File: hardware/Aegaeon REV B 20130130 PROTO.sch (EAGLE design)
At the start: 39 parts, among them IC1 ATTINY84A-MMH, Q1 DMN65D8LDW, U1 V_REG_LDOSMD

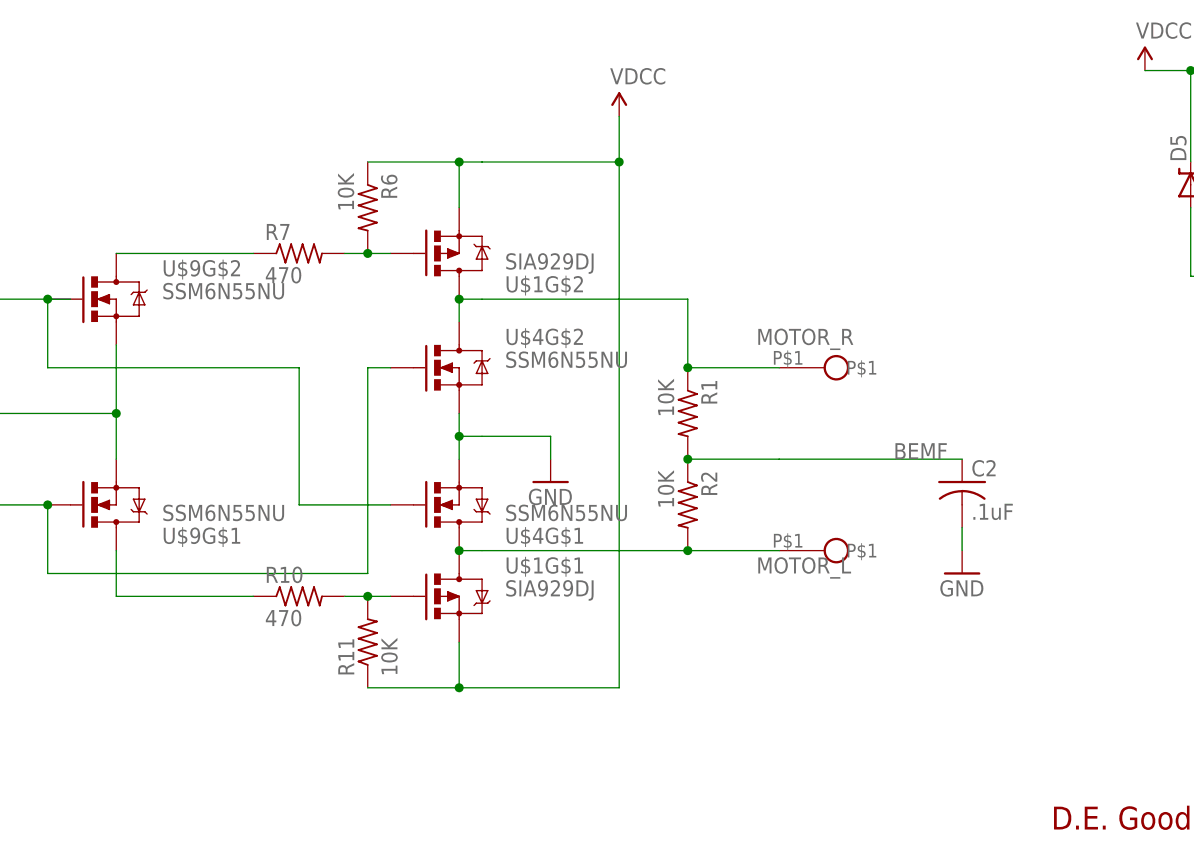
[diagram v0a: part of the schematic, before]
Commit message: Initial commit for H-Bridge designed with SI5504DC parts.
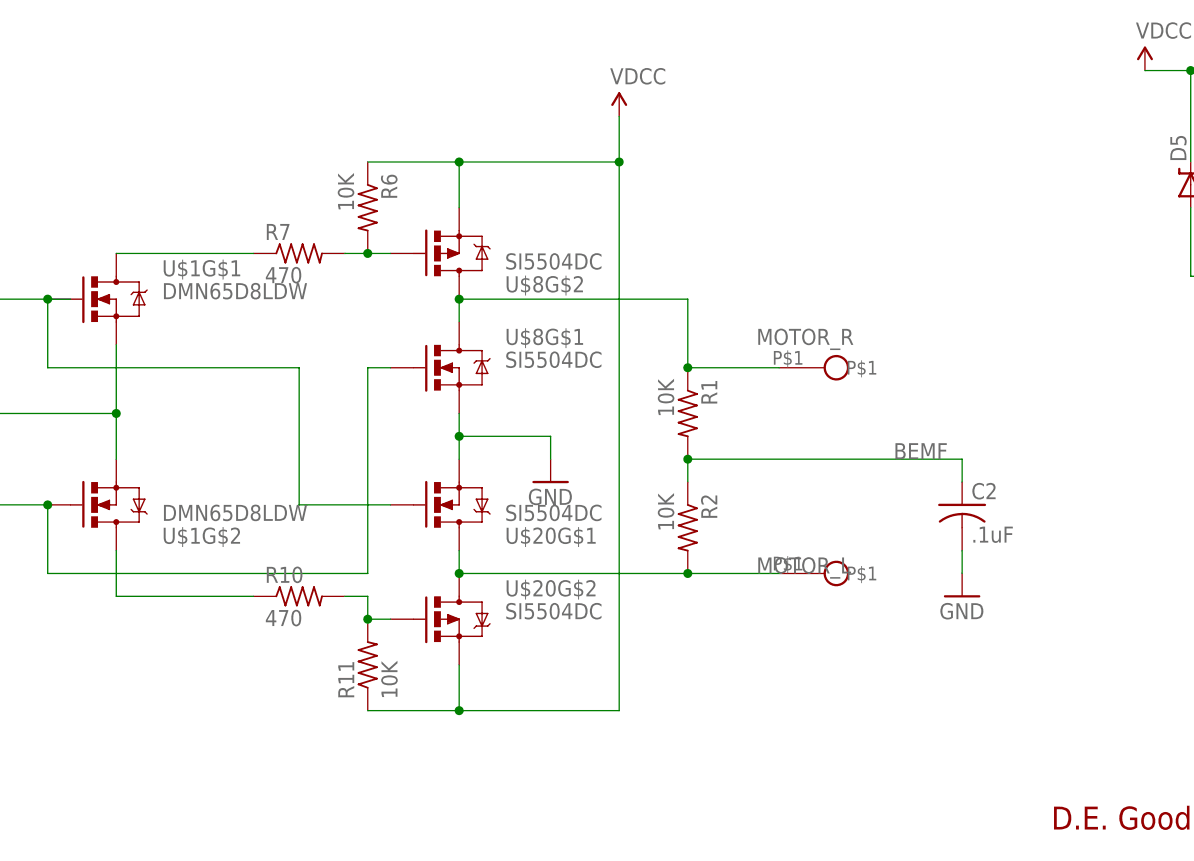
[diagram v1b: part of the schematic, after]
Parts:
- removed U$4, U$9: SSM6N55NU, Railstars:SSM6N55NU
- added U$20, U$8: SI5504DC, Railstars:SI5504DC
- U$1: value SIA929DJ -> DMN65D8LDW; device Railstars:SIA929DJ -> Railstars:DMN65D8LDW
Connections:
- net FORWARD: now also U$1G$1.G, U$20G$1.G; no longer U$4G$1.G, U$9G$2.G
- net GND: now also U$20G$1.S, U$8G$1.S; no longer U$4G$1.S, U$4G$2.S
- net MOTOR_L: now also U$20G$1.D, U$20G$2.D; no longer U$1G$1.D, U$4G$1.D
- net MOTOR_R: now also U$8G$1.D, U$8G$2.D; no longer U$1G$2.D, U$4G$2.D
- net N$1: now also U$8G$2.G; no longer U$1G$2.G
- net N$10: now also U$1G$2.D; no longer U$9G$1.D
- net N$11: now also U$1G$1.D; no longer U$9G$2.D
- net N$4: now also U$20G$2.G; no longer U$1G$1.G
- net PWM: now also U$1G$1.S, U$1G$2.S; no longer U$9G$1.S, U$9G$2.S
- net REVERSE: now also U$1G$2.G, U$8G$1.G; no longer U$4G$2.G, U$9G$1.G
- net VDCC: now also U$20G$2.S, U$8G$2.S; no longer U$1G$1.S, U$1G$2.S
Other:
- moved on the sheet: C2, R11, R2, U$1G$1, U$1G$2

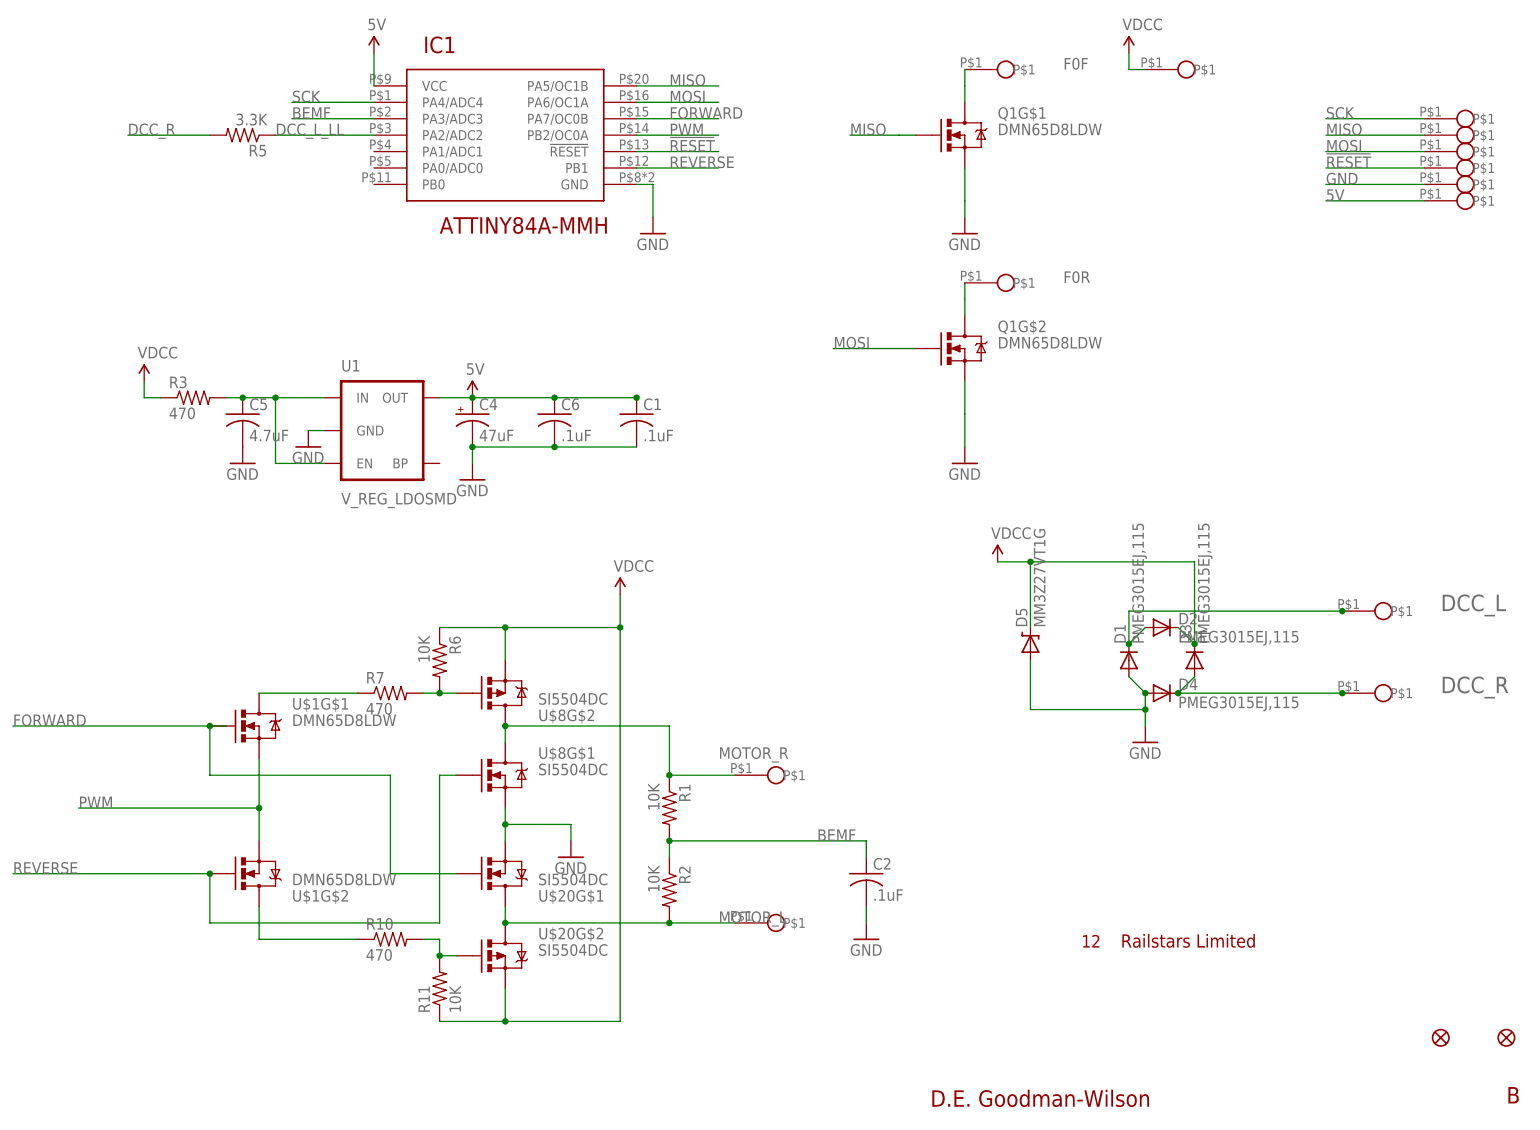
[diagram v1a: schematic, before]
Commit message: Redesigning the H-Bridge. This one seems to work under test.
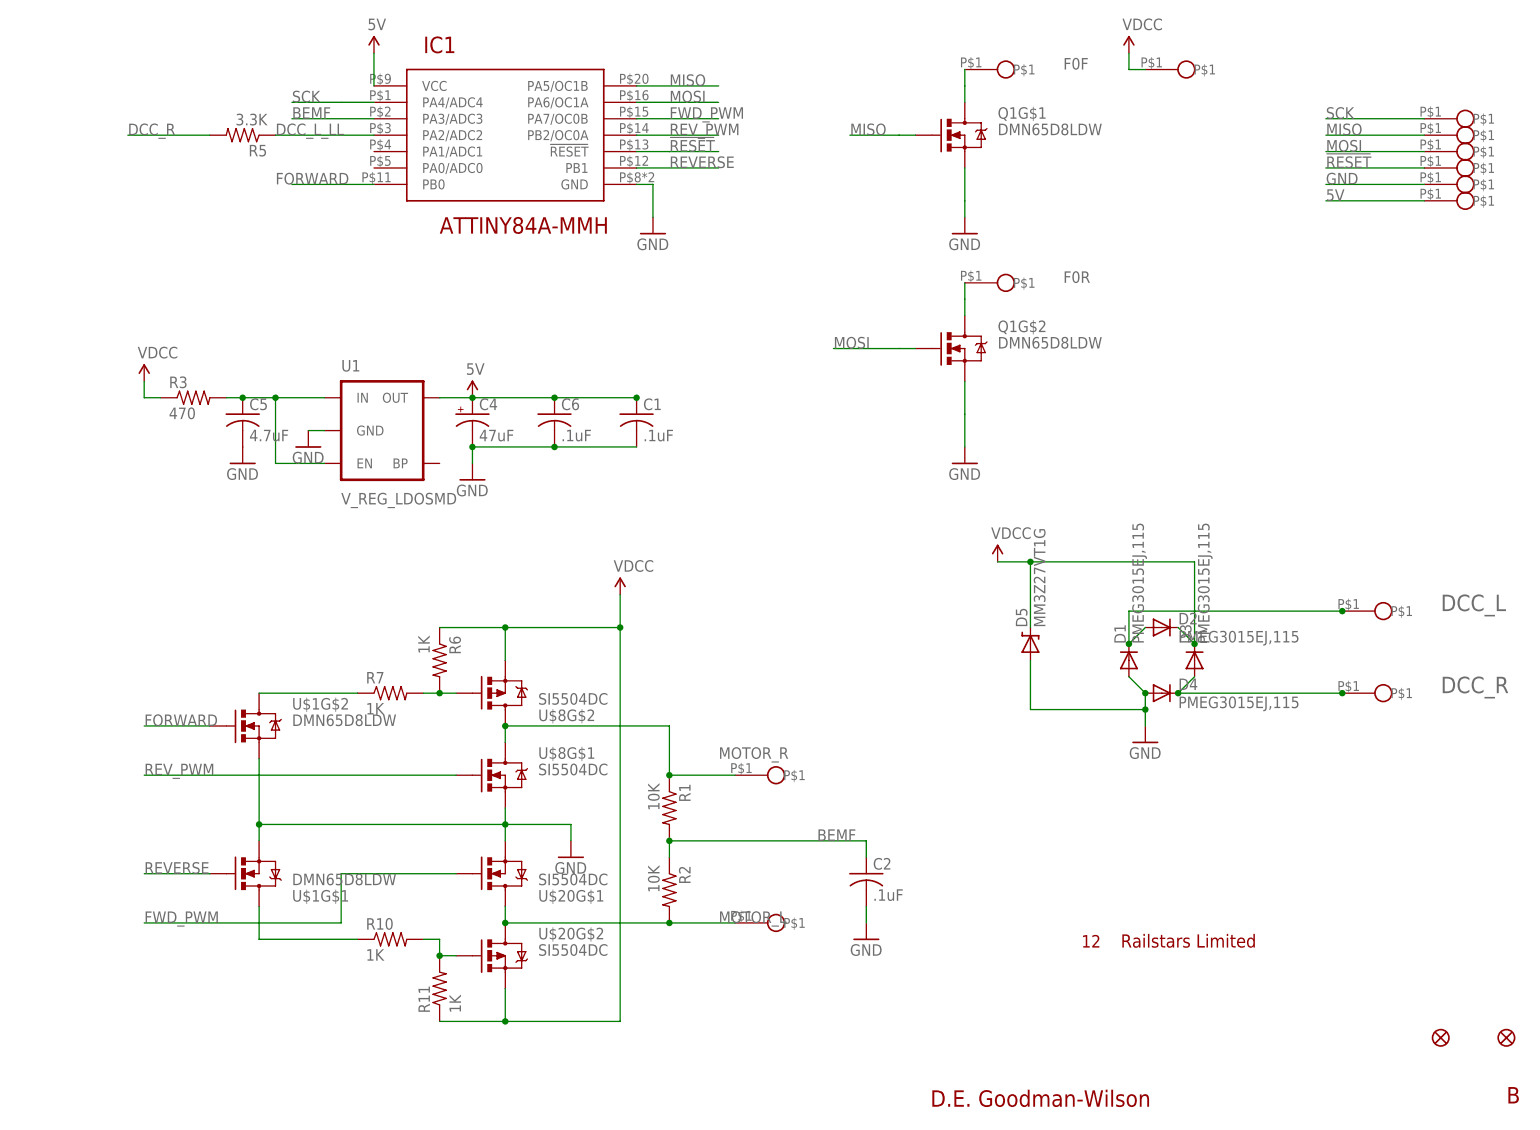
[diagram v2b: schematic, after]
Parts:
- R10, R7: value 470 -> 1K
- R11, R6: value 10K -> 1K
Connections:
- removed net PWM: IC1.PB2/OC0A, U$1G$1.S, U$1G$2.S
- new net FWD_PWM: IC1.PA7/OC0B, U$20G$1.G
- new net REV_PWM: IC1.PB2/OC0A, U$8G$1.G
- net FORWARD: now also IC1.PB0, U$1G$2.G; no longer IC1.PA7/OC0B, U$1G$1.G, U$20G$1.G
- net GND: now also U$1G$1.S, U$1G$2.S
- net N$10: now also U$1G$1.D; no longer U$1G$2.D
- net N$11: now also U$1G$2.D; no longer U$1G$1.D
- net REVERSE: now also U$1G$1.G; no longer U$1G$2.G, U$8G$1.G
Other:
- moved on the sheet: U$1G$1, U$1G$2
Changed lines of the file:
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@@
 <part name="U$7" library="Railstars" deviceset="VDCC" device=""/>
 <part name="GND8" library="SparkFun-Aesthetics" deviceset="GND" device=""/>
-<part name="R6" library="rcl" deviceset="R-US_" device="R0201" value="10K"/>
-<part name="R7" library="rcl" deviceset="R-US_" device="R0201" value="470"/>
-<part name="R10" library="rcl" deviceset="R-US_" device="R0201" value="470"/>
-<part name="R11" library="rcl" deviceset="R-US_" device="R0201" value="10K"/>
+<part name="R6" library="rcl" deviceset="R-US_" device="R0201" value="1K"/>
+<part name="R7" library="rcl" deviceset="R-US_" device="R0201" value="1K"/>
+<part name="R10" library="rcl" deviceset="R-US_" device="R0201" value="1K"/>
+<part name="R11" library="rcl" deviceset="R-US_" device="R0201" value="1K"/>
 <part name="U1" library="SparkFun-PowerIC" deviceset="V_REG_LDO" device="SMD"/>
 <part name="D5" library="SparkFun-DiscreteSemi" deviceset="DIODE-ZENER" device="-BZT52" value="MM3Z27VT1G"/>
@@
 <instance part="U$20" gate="G$1" x="83.82" y="43.18" rot="MR180"/>
 <instance part="U$20" gate="G$2" x="83.82" y="30.48"/>
-<instance part="U$1" gate="G$1" x="45.72" y="66.04"/>
-<instance part="U$1" gate="G$2" x="45.72" y="43.18" rot="MR180"/>
+<instance part="U$1" gate="G$1" x="45.72" y="43.18" rot="MR180"/>
+<instance part="U$1" gate="G$2" x="45.72" y="66.04"/>
 </instances>
 <busses>
@@
 <wire x1="83.82" y1="48.26" x2="83.82" y2="50.8" width="0.1524" layer="91"/>
 <junction x="83.82" y="50.8"/>
+<wire x1="83.82" y1="50.8" x2="45.72" y2="50.8" width="0.1524" layer="91"/>
+<pinref part="U$1" gate="G$1" pin="S"/>
+<wire x1="45.72" y1="48.26" x2="45.72" y2="50.8" width="0.1524" layer="91"/>
+<pinref part="U$1" gate="G$2" pin="S"/>
+<wire x1="45.72" y1="60.96" x2="45.72" y2="50.8" width="0.1524" layer="91"/>
+<junction x="45.72" y="50.8"/>
 </segment>
 <segment>
@@
 <net name="REVERSE" class="0">
 <segment>
-<wire x1="38.1" y1="43.18" x2="7.62" y2="43.18" width="0.1524" layer="91"/>
-<wire x1="73.66" y1="58.42" x2="73.66" y2="35.56" width="0.1524" layer="91"/>
-<wire x1="73.66" y1="35.56" x2="38.1" y2="35.56" width="0.1524" layer="91"/>
-<wire x1="38.1" y1="35.56" x2="38.1" y2="43.18" width="0.1524" layer="91"/>
-<label x="7.62" y="43.18" size="1.778" layer="95"/>
-<pinref part="U$1" gate="G$2" pin="G"/>
-<junction x="38.1" y="43.18"/>
-<pinref part="U$8" gate="G$1" pin="G"/>
-<wire x1="73.66" y1="58.42" x2="76.2" y2="58.42" width="0.1524" layer="91"/>
-</segment>
-<segment>
 <label x="109.22" y="152.4" size="1.778" layer="95"/>
 <wire x1="104.14" y1="152.4" x2="116.84" y2="152.4" width="0.1524" layer="91"/>
 <pinref part="IC1" gate="G$1" pin="PB1"/>
 </segment>
-</net>
-<net name="FORWARD" class="0">
-<segment>
-<wire x1="40.64" y1="66.04" x2="38.1" y2="66.04" width="0.1524" layer="91"/>
-<wire x1="38.1" y1="66.04" x2="7.62" y2="66.04" width="0.1524" layer="91"/>
-<wire x1="66.04" y1="43.18" x2="66.04" y2="58.42" width="0.1524" layer="91"/>
-<wire x1="66.04" y1="58.42" x2="38.1" y2="58.42" width="0.1524" layer="91"/>
-<wire x1="38.1" y1="58.42" x2="38.1" y2="66.04" width="0.1524" layer="91"/>
-<junction x="38.1" y="66.04"/>
-<label x="7.62" y="66.04" size="1.778" layer="95"/>
+<segment>
+<label x="27.94" y="43.18" size="1.778" layer="95"/>
+<wire x1="38.1" y1="43.18" x2="27.94" y2="43.18" width="0.1524" layer="91"/>
 <pinref part="U$1" gate="G$1" pin="G"/>
-<pinref part="U$20" gate="G$1" pin="G"/>
-<wire x1="76.2" y1="43.18" x2="66.04" y2="43.18" width="0.1524" layer="91"/>
-</segment>
+</segment>
+</net>
+<net name="FWD_PWM" class="0">
 <segment>
 <pinref part="IC1" gate="G$1" pin="PA7/OC0B"/>
 <wire x1="104.14" y1="160.02" x2="116.84" y2="160.02" width="0.1524" layer="91"/>
 <label x="109.22" y="160.02" size="1.778" layer="95"/>
+</segment>
+<segment>
+<pinref part="U$20" gate="G$1" pin="G"/>
+<wire x1="76.2" y1="43.18" x2="58.42" y2="43.18" width="0.1524" layer="91"/>
+<wire x1="58.42" y1="43.18" x2="58.42" y2="35.56" width="0.1524" layer="91"/>
+<wire x1="58.42" y1="35.56" x2="27.94" y2="35.56" width="0.1524" layer="91"/>
+<label x="27.94" y="35.56" size="1.778" layer="95"/>
 </segment>
 </net>
@@
 <pinref part="R10" gate="G$1" pin="1"/>
 <wire x1="45.72" y1="33.02" x2="60.96" y2="33.02" width="0.1524" layer="91"/>
-<wire x1="45.72" y1="38.1" x2="45.72" y2="33.02" width="0.1524" layer="91"/>
-<pinref part="U$1" gate="G$2" pin="D"/>
+<pinref part="U$1" gate="G$1" pin="D"/>
+<wire x1="45.72" y1="33.02" x2="45.72" y2="38.1" width="0.1524" layer="91"/>
 </segment>
 </net>
@@
 <pinref part="R7" gate="G$1" pin="1"/>
 <wire x1="45.72" y1="71.12" x2="60.96" y2="71.12" width="0.1524" layer="91"/>
-<pinref part="U$1" gate="G$1" pin="D"/>
+<pinref part="U$1" gate="G$2" pin="D"/>
 </segment>
 </net>
@@
 </segment>
 </net>
-<net name="PWM" class="0">
-<segment>
-<wire x1="45.72" y1="60.96" x2="45.72" y2="53.34" width="0.1524" layer="91"/>
-<wire x1="45.72" y1="53.34" x2="45.72" y2="48.26" width="0.1524" layer="91"/>
-<wire x1="45.72" y1="53.34" x2="17.78" y2="53.34" width="0.1524" layer="91"/>
-<junction x="45.72" y="53.34"/>
-<label x="17.78" y="53.34" size="1.778" layer="95"/>
-<pinref part="U$1" gate="G$2" pin="S"/>
-<pinref part="U$1" gate="G$1" pin="S"/>
-</segment>
+<net name="REV_PWM" class="0">
 <segment>
 <pinref part="IC1" gate="G$1" pin="PB2/OC0A"/>
@@
 <label x="109.22" y="157.48" size="1.778" layer="95"/>
 </segment>
-</net>
+<segment>
+<pinref part="U$8" gate="G$1" pin="G"/>
+<wire x1="76.2" y1="58.42" x2="27.94" y2="58.42" width="0.1524" layer="91"/>
+<label x="27.94" y="58.42" size="1.778" layer="95"/>
+</segment>
+</net>
+<net name="FORWARD" class="0">
+<segment>
+<pinref part="IC1" gate="G$1" pin="PB0"/>
+<wire x1="63.5" y1="149.86" x2="50.8" y2="149.86" width="0.1524" layer="91"/>
+<label x="48.26" y="149.86" size="1.778" layer="95"/>
+</segment>
+<segment>
+<label x="27.94" y="66.04" size="1.778" layer="95"/>
+<wire x1="38.1" y1="66.04" x2="27.94" y2="66.04" width="0.1524" layer="91"/>
+<pinref part="U$1" gate="G$2" pin="G"/>
+</segment>
+</net>
